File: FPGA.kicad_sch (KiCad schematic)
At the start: 71 parts, among them U11 IS62WV51216BLL-55TLI, U7 CAT24C128, U8 LFE5U-25F-8MG285C, U9 W25Q128JVP, X1 27MHz

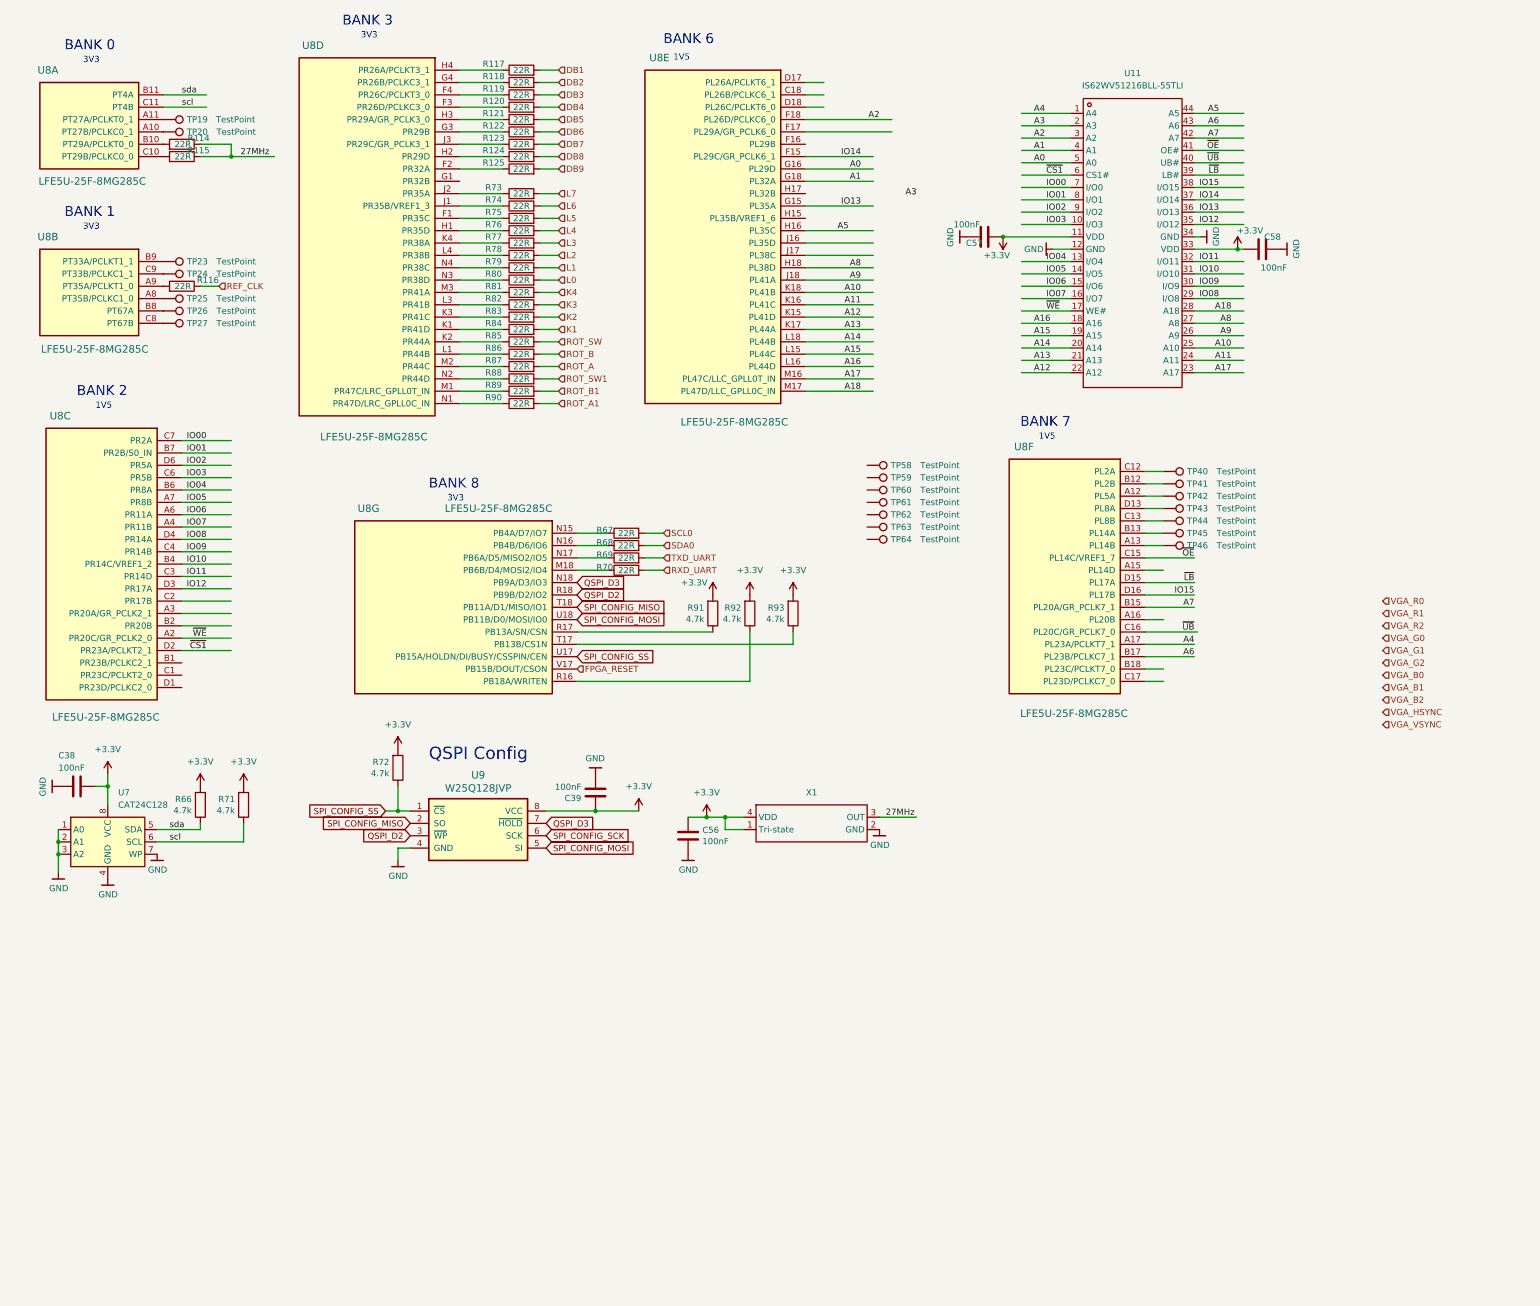
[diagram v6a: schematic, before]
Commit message: routing sram
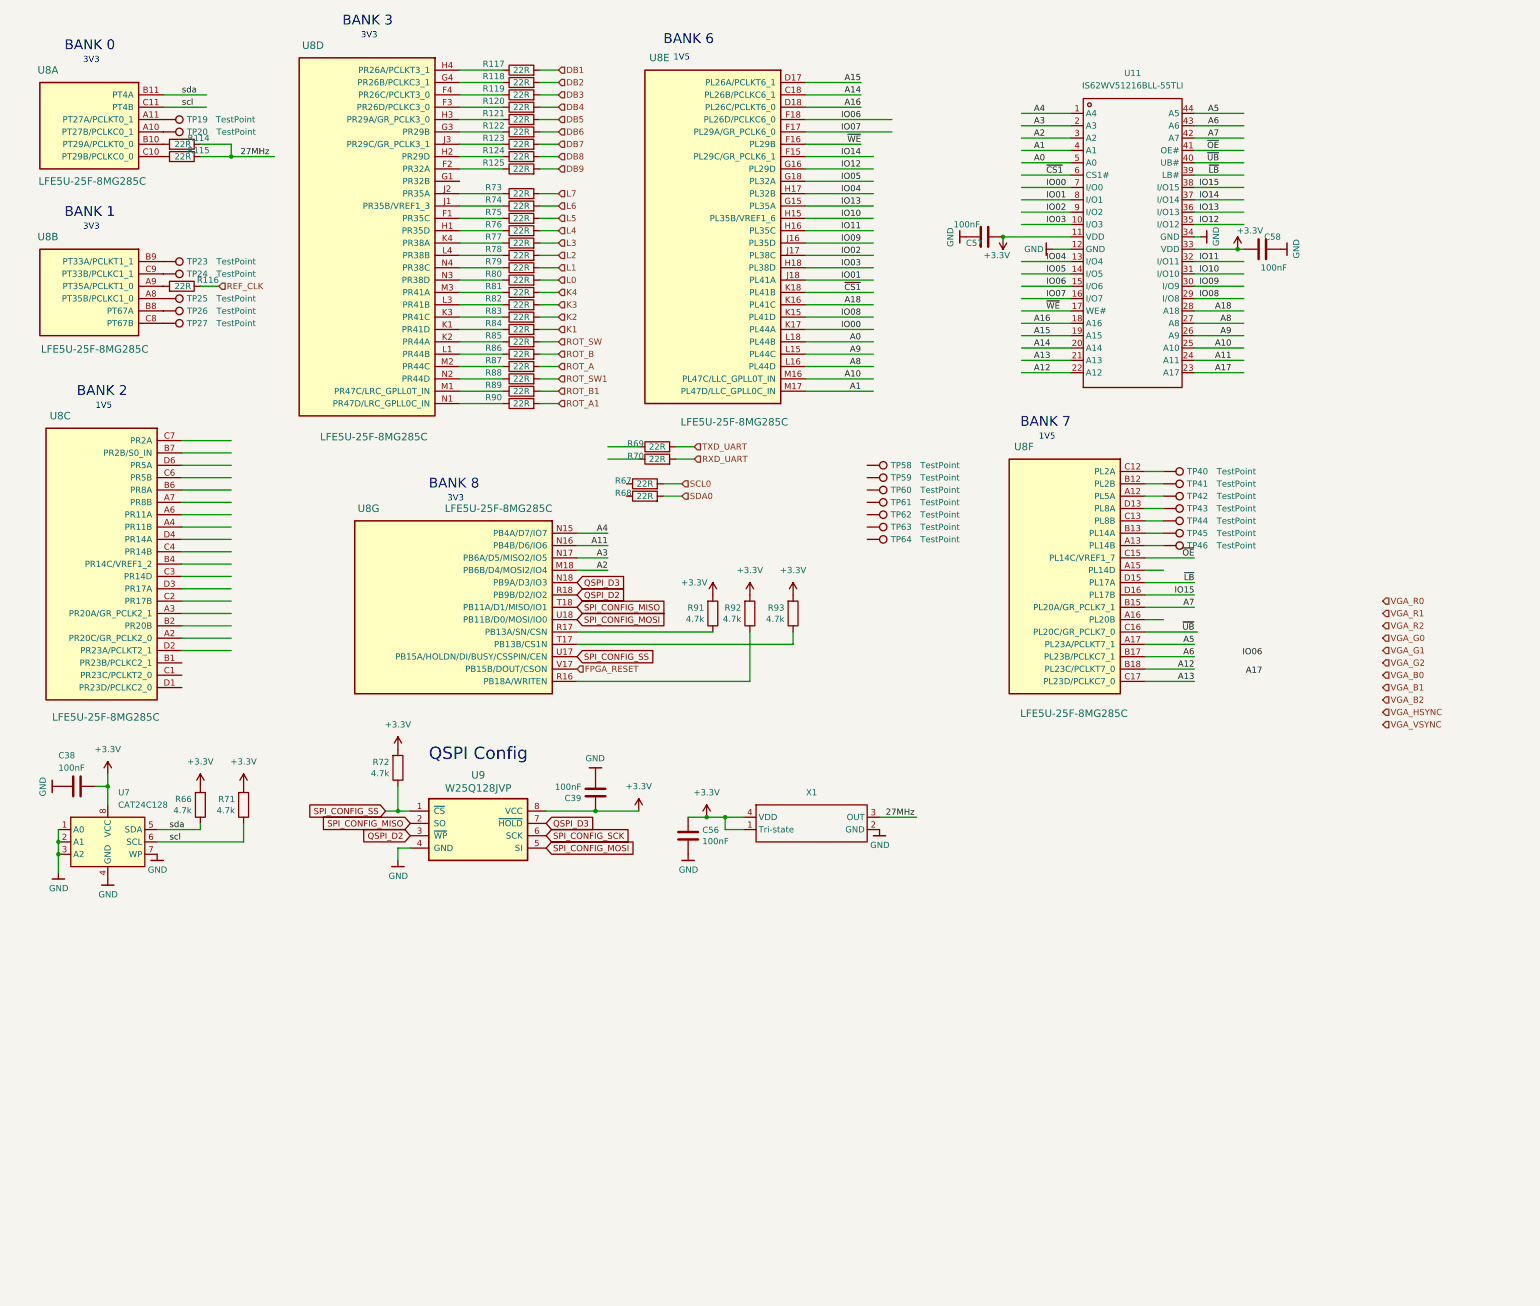
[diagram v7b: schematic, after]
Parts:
- U11: JLC_3DModel_Q (none) -> 81284d8225db4387bf18f410f83c5619; JLC_3D_Size (none) -> 11.8125 18.4
- U8: ComponentClass (none) -> fanout; LCSC (none) -> C5664013
- U9: LCSC (none) -> C190862
- X1: JLC_3DModel_Q (none) -> 3d8e5f33629249f9a4089449c02742d4; JLC_3D_Size (none) -> 3.2 2.5
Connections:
- net A0: now also U8.L18 (PL44B); no longer U8.G16 (PL29D)
- net A1: now also U8.M17 (PL47D/LLC_GPLL0C_IN); no longer U8.G18 (PL32A)
- net A10: now also U8.M16 (PL47C/LLC_GPLL0T_IN); no longer U8.K18 (PL41B)
- net A11: now also U8.N16 (PB4B/D6/IO6); no longer U8.K16 (PL41C)
- net A12: now also U8.B18 (PL23C/PCLKT7_0); no longer U8.K15 (PL41D)
- net A13: now also U8.C17 (PL23D/PCLKC7_0); no longer U8.K17 (PL44A)
- net A14: now also U8.C18 (PL26B/PCLKC6_1); no longer U8.L18 (PL44B)
- net A15: now also U8.D17 (PL26A/PCLKT6_1); no longer U8.L15 (PL44C)
- net A16: now also U8.D18 (PL26C/PCLKT6_0); no longer U8.L16 (PL44D)
- net A17: no longer U8.M16 (PL47C/LLC_GPLL0T_IN)
- net A18: now also U8.K16 (PL41C); no longer U8.M17 (PL47D/LLC_GPLL0C_IN)
- net A2: now also U8.M18 (PB6B/D4/MOSI2/IO4); no longer U8.F18 (PL26D/PCLKC6_0)
- net A3: now also U8.N17 (PB6A/D5/MISO2/IO5)
- net A4: now also U8.N15 (PB4A/D7/IO7); no longer U8.A17 (PL23A/PCLKT7_1)
- net A5: now also U8.A17 (PL23A/PCLKT7_1); no longer U8.H16 (PL35C)
- net A8: now also U8.L16 (PL44D); no longer U8.H18 (PL38D)
- net A9: now also U8.L15 (PL44C); no longer U8.J18 (PL41A)
- net IO00: now also U8.K17 (PL44A); no longer U8.C7 (PR2A)
- net IO01: now also U8.J18 (PL41A); no longer U8.B7 (PR2B/S0_IN)
- net IO02: now also U8.J17 (PL38C); no longer U8.D6 (PR5A)
- net IO03: now also U8.H18 (PL38D); no longer U8.C6 (PR5B)
- net IO04: now also U8.H17 (PL32B); no longer U8.B6 (PR8A)
- net IO05: now also U8.G18 (PL32A); no longer U8.A7 (PR8B)
- net IO06: now also U8.F18 (PL26D/PCLKC6_0); no longer U8.A6 (PR11A)
- net IO07: now also U8.F17 (PL29A/GR_PCLK6_0); no longer U8.A4 (PR11B)
- net IO08: now also U8.K15 (PL41D); no longer U8.D4 (PR14A)
- net IO09: now also U8.J16 (PL35D); no longer U8.C4 (PR14B)
- net IO10: now also U8.H15 (PL35B/VREF1_6); no longer U8.B4 (PR14C/VREF1_2)
- net IO11: now also U8.H16 (PL35C); no longer U8.C3 (PR14D)
- net IO12: now also U8.G16 (PL29D); no longer U8.D3 (PR17A)
- net ~{CS1}: now also U8.K18 (PL41B); no longer U8.D2 (PR23A/PCLKT2_1)
- net ~{WE}: now also U8.F16 (PL29B); no longer U8.A2 (PR20C/GR_PCLK2_0)
- net at R70.1: no longer U8.M18 (PB6B/D4/MOSI2/IO4)
- net at R67.1: no longer U8.N15 (PB4A/D7/IO7)
- net at R68.1: no longer U8.N16 (PB4B/D6/IO6)
- net at R69.1: no longer U8.N17 (PB6A/D5/MISO2/IO5)
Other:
- moved on the sheet: R67, R68, R69, R70

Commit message: Routing sram
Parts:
- added R126, R127, R128, R129, R130, R131, R132, R133, R134, R135, R136, R137, R138, R139, R140, R141, R142, R143, R144, R145, R146, R147, R148, R149, R150, R151, R152, R153, R154, R155, R156, R157, R158, R159, R160, R161, R162, R163, R164, R165: 22R, Resistor_SMD:R_01005_0402Metric_Pad0.57x0.30mm_HandSolder, symbol Device:R
- R114, R115, R116, R117, R118, R119, R120, R121, R122, R123, R124, R125, R67, R68, R69, R70, R73, R74, R75, R76, R77, R78, R79, R80, R81, R82, R83, R84, R85, R86, R87, R88, R89, R90: footprint Resistor_SMD:R_0603_1608Metric -> Resistor_SMD:R_01005_0402Metric_Pad0.57x0.30mm_HandSolder
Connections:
- net A0: now also R151.2; no longer U8.L18 (PL44B)
- net A1: now also R155.2; no longer U8.M17 (PL47D/LLC_GPLL0C_IN)
- net A10: now also R154.2; no longer U8.M16 (PL47C/LLC_GPLL0T_IN)
- net A11: now also R127.2; no longer U8.N16 (PB4B/D6/IO6)
- net A12: now also R164.2; no longer U8.B18 (PL23C/PCLKT7_0)
- net A13: now also R165.2; no longer U8.C17 (PL23D/PCLKC7_0)
- net A14: now also R131.2; no longer U8.C18 (PL26B/PCLKC6_1)
- net A15: now also R130.2; no longer U8.D17 (PL26A/PCLKT6_1)
- net A16: now also R132.2; no longer U8.D18 (PL26C/PCLKT6_0)
- net A17: now also R163.2
- net A18: now also R148.2; no longer U8.K16 (PL41C)
- net A2: now also R129.2; no longer U8.M18 (PB6B/D4/MOSI2/IO4)
- net A3: now also R128.2; no longer U8.N17 (PB6A/D5/MISO2/IO5)
- net A4: now also R126.2; no longer U8.N15 (PB4A/D7/IO7)
- net A5: now also R160.2; no longer U8.A17 (PL23A/PCLKT7_1)
- net A6: now also R162.2; no longer U8.B17 (PL23B/PCLKC7_1)
- net A7: now also R159.2; no longer U8.B15 (PL20A/GR_PCLK7_1)
- net A8: now also R153.2; no longer U8.L16 (PL44D)
- net A9: now also R152.2; no longer U8.L15 (PL44C)
- net IO00: now also R150.2; no longer U8.K17 (PL44A)
- net IO01: now also R146.2; no longer U8.J18 (PL41A)
- net IO02: now also R144.2; no longer U8.J17 (PL38C)
- net IO03: now also R145.2; no longer U8.H18 (PL38D)
- net IO04: now also R139.2; no longer U8.H17 (PL32B)
- net IO05: now also R138.2; no longer U8.G18 (PL32A)
- net IO06: now also R133.2; no longer U8.F18 (PL26D/PCLKC6_0)
- net IO07: now also R134.2; no longer U8.F17 (PL29A/GR_PCLK6_0)
- net IO08: now also R149.2; no longer U8.K15 (PL41D)
- net IO09: now also R143.2; no longer U8.J16 (PL35D)
- net IO10: now also R141.2; no longer U8.H15 (PL35B/VREF1_6)
- net IO11: now also R142.2; no longer U8.H16 (PL35C)
- net IO12: now also R137.2; no longer U8.G16 (PL29D)
- net IO13: now also R140.2; no longer U8.G15 (PL35A)
- net IO14: now also R136.2; no longer U8.F15 (PL29C/GR_PCLK6_1)
- net IO15: now also R158.2; no longer U8.D16 (PL17B)
- net VGA_B0: now also U8.A2 (PR20C/GR_PCLK2_0)
- net VGA_B1: now also U8.D2 (PR23A/PCLKT2_1)
- net VGA_B2: now also U8.B1 (PR23B/PCLKC2_1)
- net VGA_G0: now also U8.C2 (PR17B)
- net VGA_G1: now also U8.A3 (PR20A/GR_PCLK2_1)
- net VGA_G2: now also U8.B2 (PR20B)
- net VGA_HSYNC: now also U8.C1 (PR23C/PCLKT2_0)
- net VGA_R0: now also U8.B4 (PR14C/VREF1_2)
- net VGA_R1: now also U8.C3 (PR14D)
- net VGA_R2: now also U8.D3 (PR17A)
- net VGA_VSYNC: now also U8.D1 (PR23D/PCLKC2_0)
- net ~{CS1}: now also R147.2; no longer U8.K18 (PL41B)
- net ~{LB}: now also R157.2; no longer U8.D15 (PL17A)
- net ~{OE}: now also R156.2; no longer U8.C15 (PL14C/VREF1_7)
- net ~{UB}: now also R161.2; no longer U8.C16 (PL20C/GR_PCLK7_0)
- net ~{WE}: now also R135.2; no longer U8.F16 (PL29B)
- net at U8.A16 (PL20B): now also R160.1
- new net: R163.1, U8.C18 (PL26B/PCLKC6_1)
- new net: R130.1, U8.D17 (PL26A/PCLKT6_1)
- new net: R132.1, U8.D18 (PL26C/PCLKT6_0)
- new net: R136.1, U8.F15 (PL29C/GR_PCLK6_1)
- new net: R135.1, U8.F16 (PL29B)
- new net: R134.1, U8.F17 (PL29A/GR_PCLK6_0)
- new net: R133.1, U8.F18 (PL26D/PCLKC6_0)
- new net: R140.1, U8.G15 (PL35A)
- new net: R137.1, U8.G16 (PL29D)
- new net: R138.1, U8.G18 (PL32A)
- new net: R141.1, U8.H15 (PL35B/VREF1_6)
- new net: R142.1, U8.H16 (PL35C)
- new net: R139.1, U8.H17 (PL32B)
- new net: R145.1, U8.H18 (PL38D)
- new net: R143.1, U8.J16 (PL35D)
- new net: R144.1, U8.J17 (PL38C)
- new net: R146.1, U8.J18 (PL41A)
- new net: R149.1, U8.K15 (PL41D)
- new net: R148.1, U8.K16 (PL41C)
- new net: R150.1, U8.K17 (PL44A)
- new net: R147.1, U8.K18 (PL41B)
- new net: R152.1, U8.L15 (PL44C)
- new net: R153.1, U8.L16 (PL44D)
- new net: R151.1, U8.L18 (PL44B)
- new net: R154.1, U8.M16 (PL47C/LLC_GPLL0T_IN)
- new net: R155.1, U8.M17 (PL47D/LLC_GPLL0C_IN)
- new net: R162.1, U8.A17 (PL23A/PCLKT7_1)
- new net: R159.1, U8.B15 (PL20A/GR_PCLK7_1)
- new net: R131.1, U8.B17 (PL23B/PCLKC7_1)
- new net: R164.1, U8.B18 (PL23C/PCLKT7_0)
- new net: R156.1, U8.C15 (PL14C/VREF1_7)
- new net: R161.1, U8.C16 (PL20C/GR_PCLK7_0)
- new net: R165.1, U8.C17 (PL23D/PCLKC7_0)
- new net: R157.1, U8.D15 (PL17A)
- new net: R158.1, U8.D16 (PL17B)
- new net: R129.1, U8.M18 (PB6B/D4/MOSI2/IO4)
- new net: R126.1, U8.N15 (PB4A/D7/IO7)
- new net: R127.1, U8.N16 (PB4B/D6/IO6)
- new net: R128.1, U8.N17 (PB6A/D5/MISO2/IO5)
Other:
- moved on the sheet: TP40, TP41, TP42, TP43, TP44, TP45, TP46, TP58, TP59, TP60, TP61, TP62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
